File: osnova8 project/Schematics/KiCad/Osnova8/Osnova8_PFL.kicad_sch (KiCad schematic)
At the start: 14 parts, among them U19 74LS670, U20 74LS374, U21 74LS541, U22 74LS670, U23 74LS283, U24 74LS283, U25 74LS541

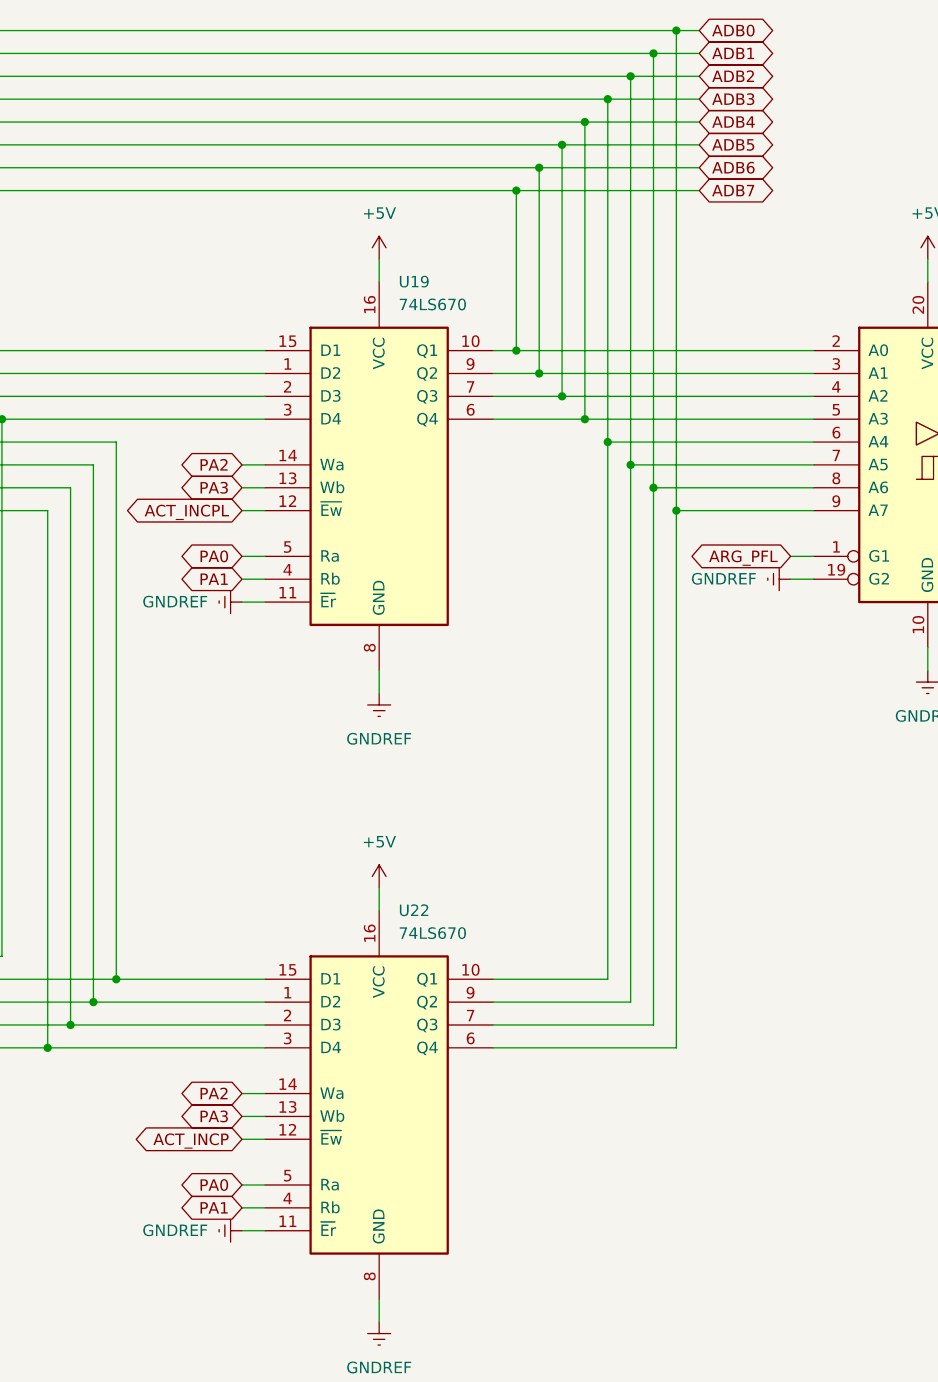
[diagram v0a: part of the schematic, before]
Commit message: updated schematics
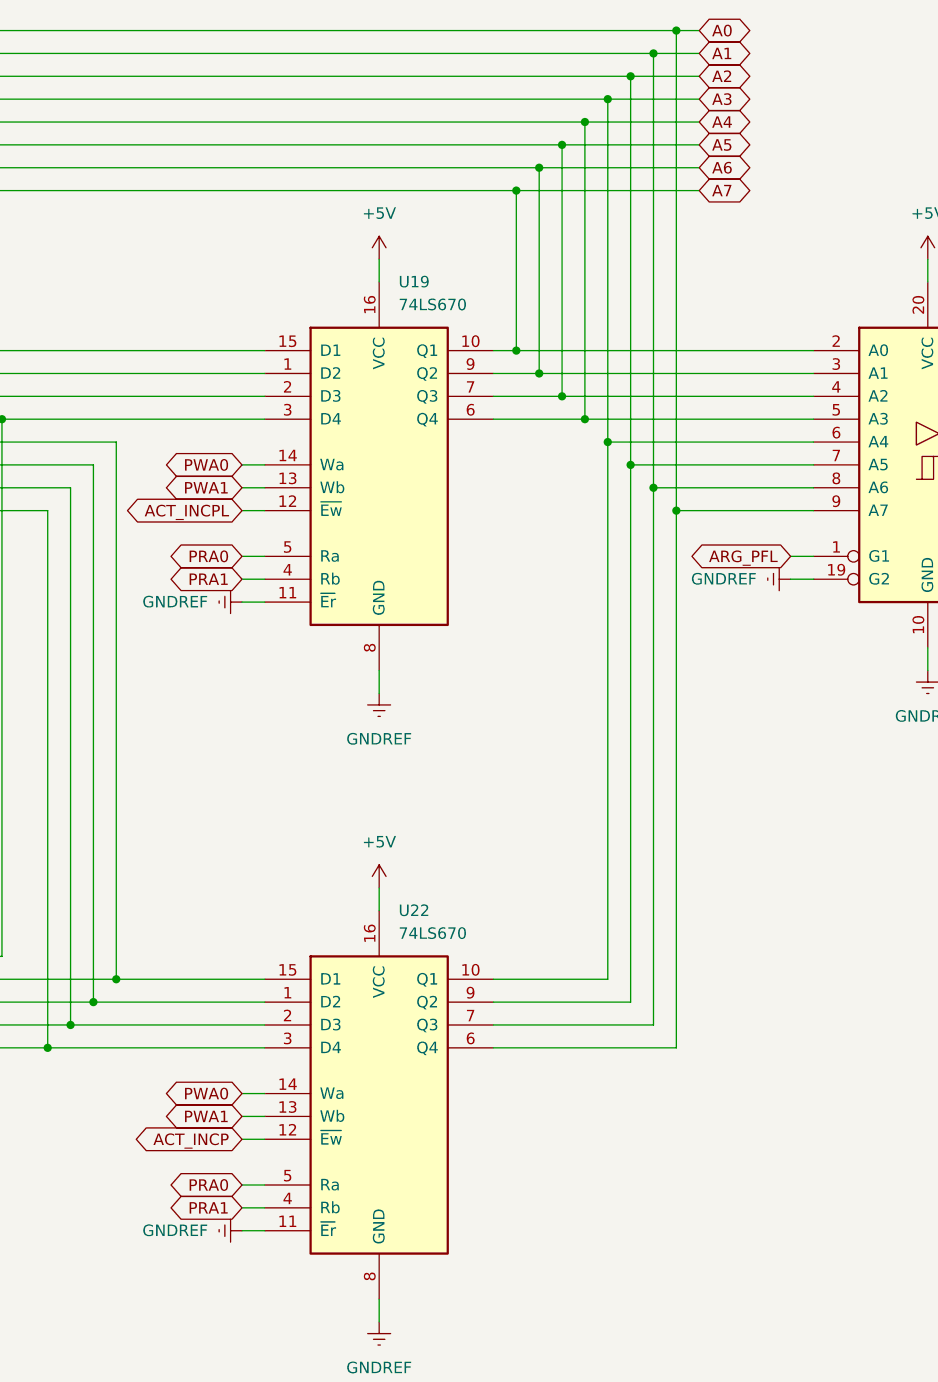
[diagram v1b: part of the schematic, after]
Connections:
- net ADB0 renamed A0
- net ADB1 renamed A1
- net ADB2 renamed A2
- net ADB3 renamed A3
- net ADB4 renamed A4
- net ADB5 renamed A5
- net ADB6 renamed A6
- net ADB7 renamed A7
- net PA0 renamed PRA0
- net PA1 renamed PRA1
- net PA2 renamed PWA0
- net PA3 renamed PWA1
